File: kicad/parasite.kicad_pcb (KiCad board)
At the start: 2 copper layers, 22 x 126.4 mm, 33 parts, among them Q1 MMBT3904, Q2 MMBT3904, Q3 AO3407, Q4 Q_Photo_NPN, U1 E73-2G4M08S1C-52840, U2 SHTC3, Y1 32.768kHz

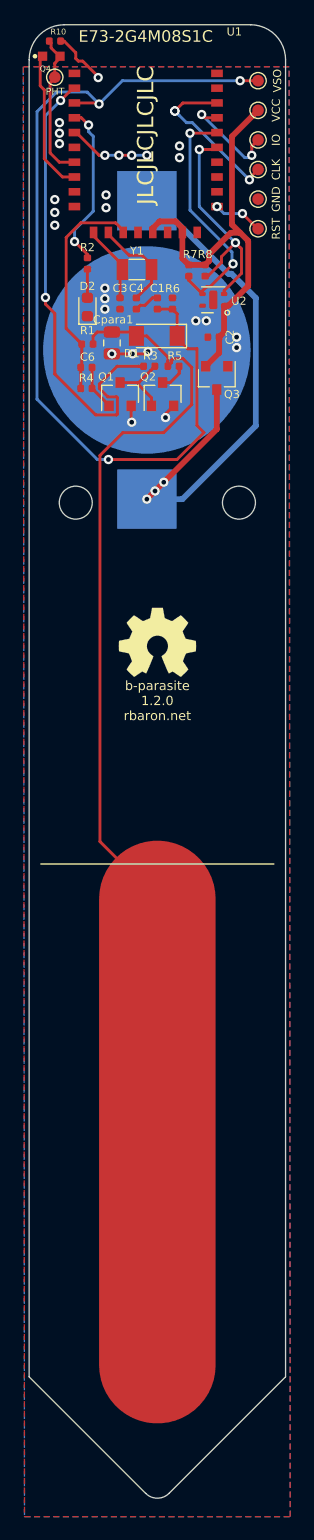
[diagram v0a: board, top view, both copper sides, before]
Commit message: 4 layer version
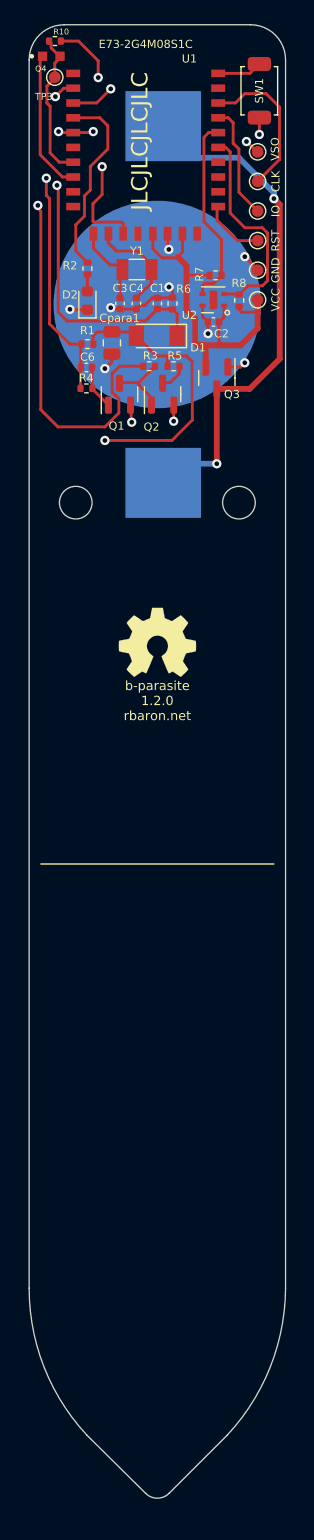
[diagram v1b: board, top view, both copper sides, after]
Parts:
- added H1: MountingHole, Library:MountingHole_2.8mm, B.Cu at (61.0, 68.2)
- added H2: MountingHole, Library:MountingHole_2.8mm, F.Cu at (75.0, 68.0)
- added SW1: SKRKAEE020, Library:SW_Push_SPST_NO_Alps_SKRK, F.Cu at (76.8, 32.7)
- BT1: footprint kicad:BatteryHolder_Keystone_3002_1x2032 -> Library:BatteryHolder_combined
- U1: footprint nrfmicro:E73-2G4M08S1C-52840 -> Library:E73-2G4M08S1C-52840
- moved TP7 16.3 mm to (76.6, 50.6)
- moved TP6 6.10 mm to (76.6, 48.1)
- moved TP4 6.10 mm to (76.6, 37.9)
- moved TP1 6.10 mm to (76.6, 43.0)
- moved BT1 4.00 mm to (68.0, 51.0)
- moved R8 3.89 mm to (75.0, 50.6), turned to 90 degrees
- moved R7 2.34 mm to (73.0, 48.5), turned to 180 degrees
- moved C2 1.30 mm to (72.8, 52.5)
- moved TP5 1.02 mm to (76.6, 45.5)
- moved TP2 1.02 mm to (76.6, 40.4)
- moved D2 0.55 mm to (62.0, 50.7)
- moved R2 0.43 mm to (62.0, 47.9)
- renumbered PHT to TP3
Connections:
- U1 pad 1: Net-(U1-Pad1) -> unconnected-(U1-Pad1)
- U1 pad 10: Net-(U1-Pad10) -> unconnected-(U1-Pad10)
- U1 pad 17: Net-(U1-Pad17) -> unconnected-(U1-Pad17)
- U1 pad 25: Net-(U1-Pad25) -> unconnected-(U1-Pad25)
- U1 pad 27: Net-(U1-Pad27) -> unconnected-(U1-Pad27)
- U1 pad 29: Net-(U1-Pad29) -> unconnected-(U1-Pad29)
- U1 pad 31: Net-(U1-Pad31) -> unconnected-(U1-Pad31)
- U1 pad 41: Net-(U1-Pad41) -> unconnected-(U1-Pad41)
- U1 pad 43: Net-(U1-Pad43) -> /SW
- U1 pad 6: Net-(U1-Pad6) -> unconnected-(U1-Pad6)
- U1 pad 9: Net-(U1-Pad9) -> unconnected-(U1-Pad9)
- U2 pad 5: Net-(U2-Pad5) -> unconnected-(U2-Pad5)
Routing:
- net /SENS_OUT: track 78.6 -> 52.6 mm
- net /PWM: track 19.4 -> 35.2 mm, vias 0 -> 2
- net GND: track 20.4 -> 29.3 mm, vias 27 -> 14
- net Net-(BT1-Pad1): track 47.6 -> 38.8 mm, vias 3 -> 2
- net +3V0: track 37.8 -> 32.5 mm
- net /SDA: track 20.9 -> 16.5 mm, vias 2 -> 0
- net /SW: track 0.00 -> 3.86 mm
- net /FAST_DISCH_EN: track 40.9 -> 43.8 mm
- net /LED: track 14.2 -> 16.4 mm, vias 2 -> 0
- net /Csen+: track 104.6 -> 106.8 mm, vias 0 -> 1
- net /SCL: track 20.2 -> 18.5 mm, vias 2 -> 0
- net Net-(TP2-Pad1): track 14.5 -> 13.3 mm, vias 3 -> 0
- net Net-(TP5-Pad1): track 4.31 -> 5.38 mm, vias 2 -> 0
- net Net-(D2-Pad2): track 2.45 -> 1.45 mm
- net Net-(TP1-Pad1): track 8.89 -> 9.80 mm, vias 2 -> 0
- added copper zone on In2.Cu, net GND
- removed copper zone on B.Cu, net GND
- removed copper zone on F.Cu, net GND
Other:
- outline, holes or cut-outs redrawn
- copper layers 2 -> 4
